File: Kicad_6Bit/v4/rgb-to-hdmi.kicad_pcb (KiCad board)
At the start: 2 copper layers, 65 x 30 mm, 31 parts, among them P1 CONN_02X20, P2 Conn_02x06_Odd_Even, P4 CONN_01X02, P5 Conn_02x05_Odd_Even, SW1 SW_PUSH, SW2 SW_PUSH, SW3 SW_PUSH, SW4 SW_PUSH, U1 XC9572XL-VQFP44

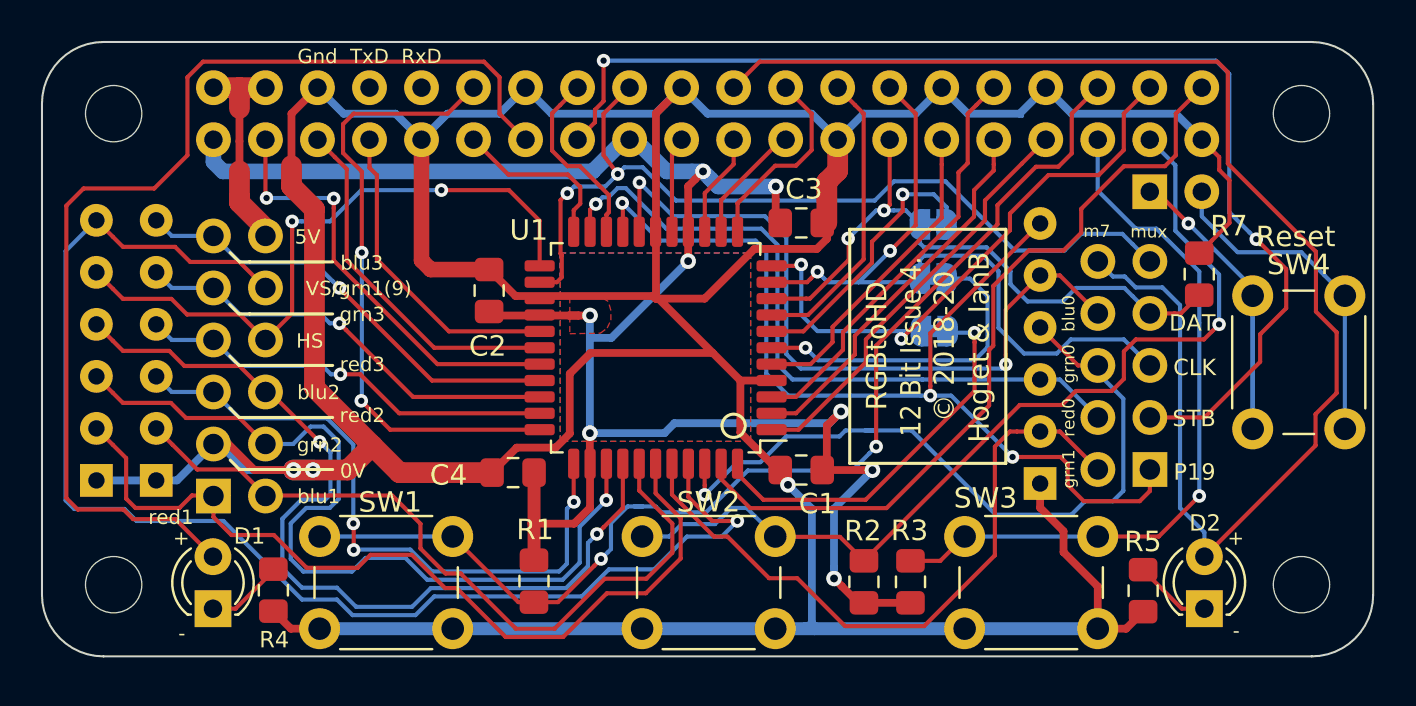
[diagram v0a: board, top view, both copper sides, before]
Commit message: Moved most component values from the Fab. Layer to the Silk Layer on the analog board and the 12-bit board to serve as an aid when placing the componets during assembly.
Generated interactive Bill Of Materials for the analog board and the 12-bit board to serve as an aid when
sourcing components and assembly.These are in the "bom" directory.

Replaced the Gerber files for the analog board and the 12-bit board with the updated silk screens.
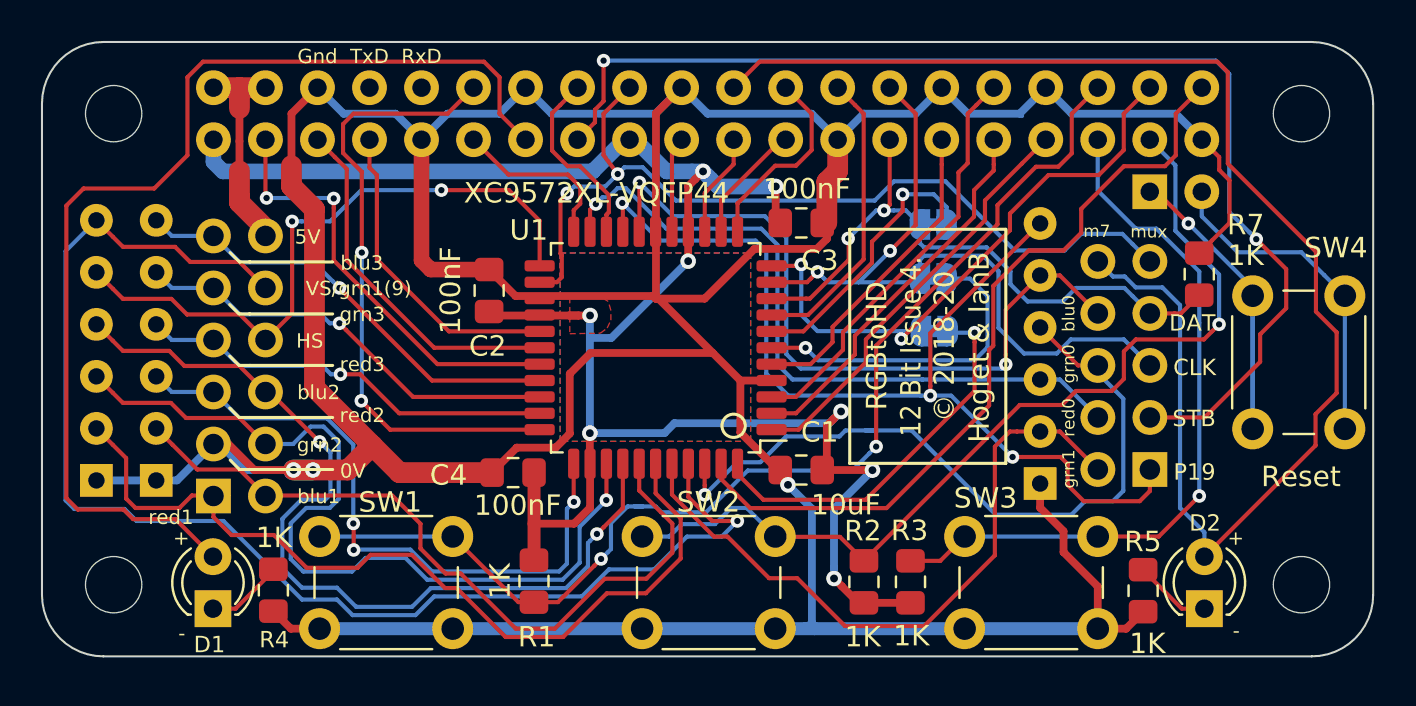
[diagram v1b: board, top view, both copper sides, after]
